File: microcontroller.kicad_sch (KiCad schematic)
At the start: 6 parts

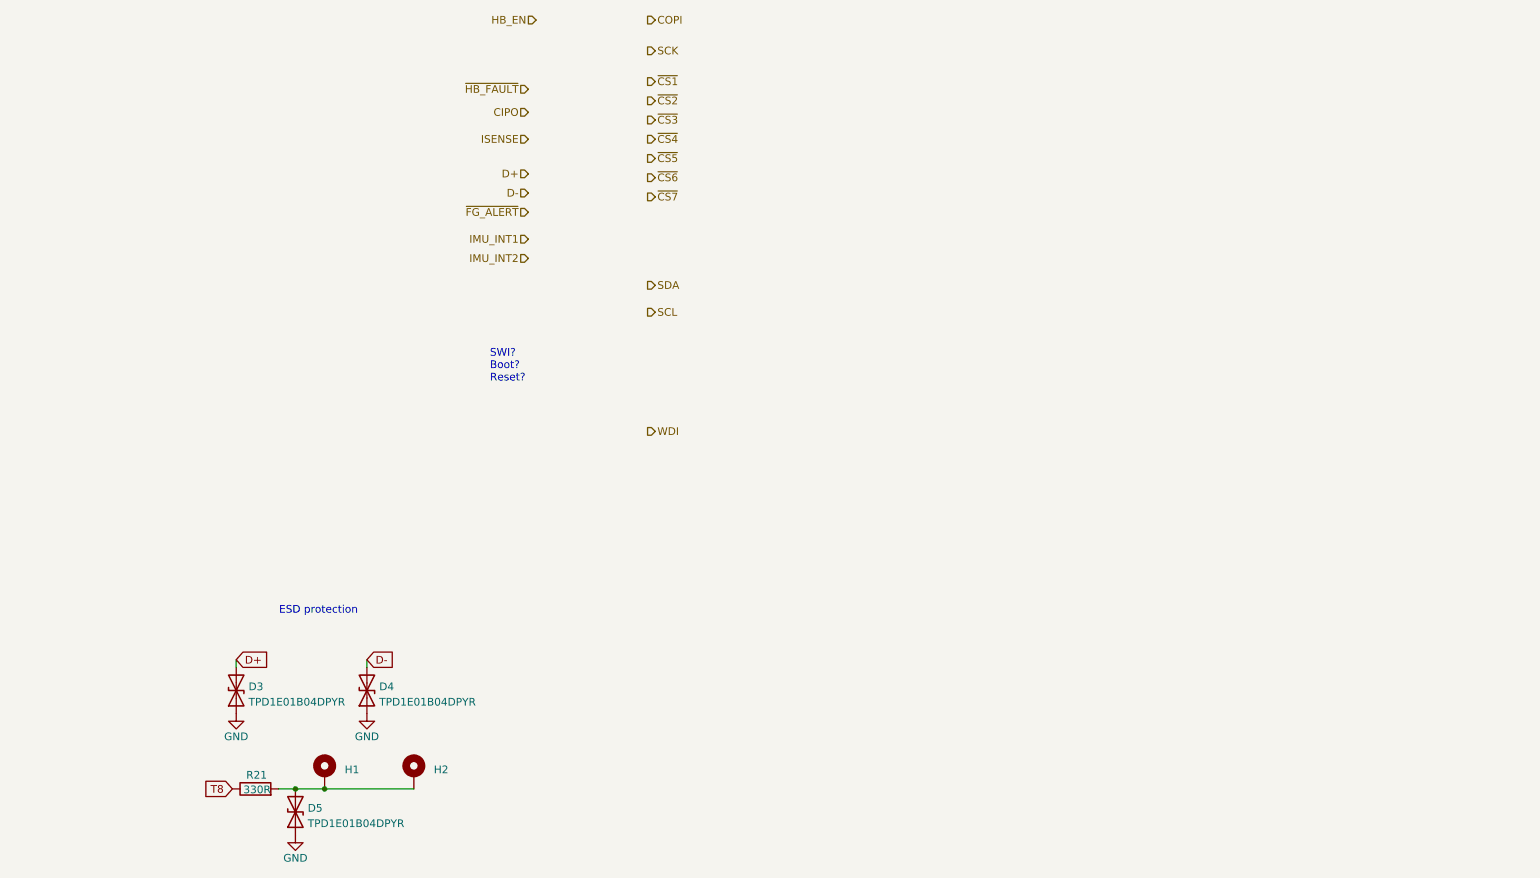
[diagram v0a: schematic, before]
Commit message: schematic rough draft except fpc
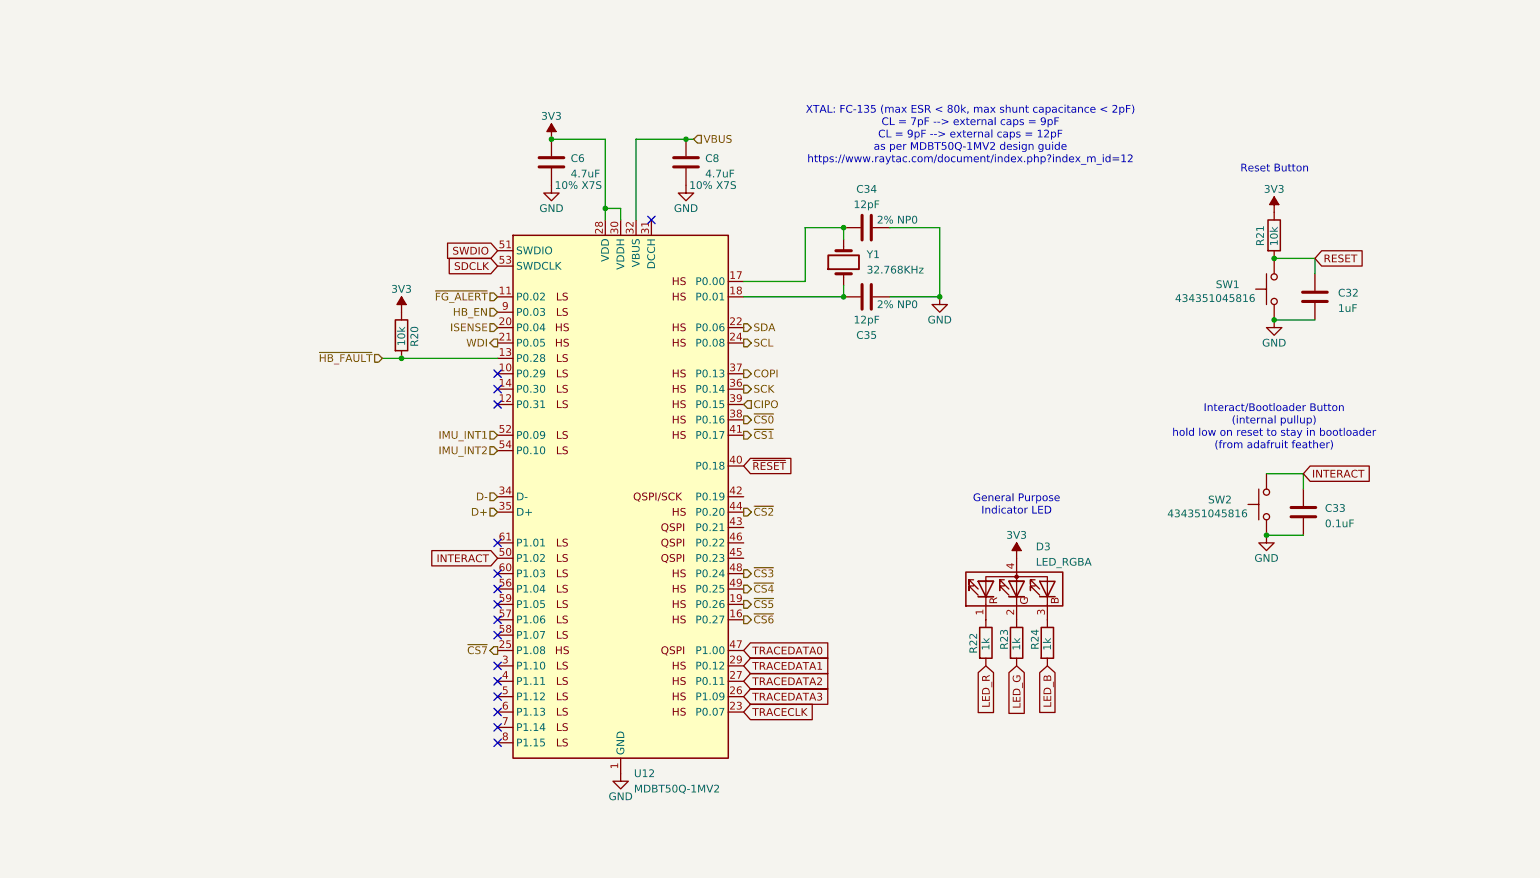
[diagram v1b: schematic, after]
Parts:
- removed D3, D4, D5: TPD1E01B04DPYR, v12e:X1-SON-2(0.6x1), symbol Device:D_TVS
- removed H1, H2: MountingHole_Pad, v12e:MountingHole_1.8mm_M1.6_Pad_TopBottom, symbol Mechanical:MountingHole_Pad
- added C32: 1uF, Capacitor_SMD:C_0402_1005Metric, symbol Device:C
- added C33: 0.1uF, Capacitor_SMD:C_0402_1005Metric, symbol Device:C
- added C34, C35: 12pF, symbol Device:C
- added C6, C8: 4.7uF, Capacitor_SMD:C_0603_1608Metric, symbol Device:C
- added D3: LED_RGBA, v12e:RGBA_LTST-S310F3WT, symbol Device:LED_RGBA
- added R20: 10k, Resistor_SMD:R_0402_1005Metric, symbol Device:R
- added R22, R23, R24: 1k, Resistor_SMD:R_0402_1005Metric, symbol Device:R
- added SW1, SW2: 434351045816, v12e:SW_Wurth_434351045816, symbol Switch:SW_Push
- added U12: MDBT50Q-1MV2, RF_Module:Raytac_MDBT50Q, symbol RF_Module:MDBT50Q-1MV2
- added Y1: 32.768KHz, Crystal:Crystal_SMD_3215-2Pin_3.2x1.5mm, symbol Device:Crystal
- R21: value 330R -> 10k; JLCPCB Part # C25104 -> C25744
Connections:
- net CIPO: now also U12.39 (P0.15)
- net COPI: now also U12.37 (P0.13)
- net D+: now also U12.35 (D+)
- net D-: now also U12.34 (D-)
- net GND: now also C32.2, C33.2, C34.2, C35.1, C6.2, C8.2, SW1.1, SW2.1, U12.1 (GND), U12.15 (GND), U12.2 (GND), U12.33 (GND), U12.55 (GND)
- net HB_EN: now also U12.9 (P0.03)
- net IMU_INT1: now also U12.52 (P0.09)
- net IMU_INT2: now also U12.54 (P0.10)
- net ISENSE: now also U12.20 (P0.04)
- net SCK: now also U12.36 (P0.14)
- net SCL: now also U12.24 (P0.08)
- net SDA: now also U12.22 (P0.06)
- net WDI: now also U12.21 (P0.05)
- net ~{CS1}: now also U12.41 (P0.17)
- net ~{CS2}: now also U12.44 (P0.20)
- net ~{CS3}: now also U12.48 (P0.24)
- net ~{CS4}: now also U12.49 (P0.25)
- net ~{CS5}: now also U12.19 (P0.26)
- net ~{CS6}: now also U12.16 (P0.27)
- net ~{CS7}: now also U12.25 (P1.08)
- net ~{FG_ALERT}: now also U12.11 (P0.02)
- net ~{HB_FAULT}: now also R20.2, U12.13 (P0.28)
- net RESET: now reaches R21.2
- net RESET: now also C32.1, SW1.2
- net T8 renamed 3V3
- net 3V3: now also C6.1, D3.4 (A), R20.1, U12.28 (VDD), U12.30 (VDDH)
- new net: D3.1 (RK), R22.1
- new net: C35.2, U12.18 (P0.01), Y1.1
- new net: C34.1, U12.17 (P0.00), Y1.2
- new net: D3.2 (GK), R23.1
- new net: D3.3 (BK), R24.1
- new net INTERACT: C33.1, SW2.2, U12.50 (P1.02)
- new net LED_B: R24.2
- new net LED_G: R23.2
- new net LED_R: R22.2
- new net SDCLK: U12.53 (SWDCLK)
- new net SWDIO: U12.51 (SWDIO)
- new net TRACECLK: U12.23 (P0.07)
- new net TRACEDATA0: U12.47 (P1.00)
- new net TRACEDATA1: U12.29 (P0.12)
- new net TRACEDATA2: U12.27 (P0.11)
- new net TRACEDATA3: U12.26 (P1.09)
- new net VBUS: C8.1, U12.32 (VBUS)
- new net ~{CS0}: U12.38 (P0.16)
- new net ~{RESET}: U12.40 (P0.18)
- no-connect marks 0 -> 16
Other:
- note added: "General Purpose Indicator LED"
- note added: "Interact/Bootloader Button (internal pullup) hold low on reset to stay in bootloader (from adafruit feather)"
- note added: "Reset Button"
- note added: "XTAL: FC-135 (max ESR < 80k, max shunt capacitance < 2pF) CL = 7pF --> external caps = 9pF CL = 9pF --> external caps = 12pF as per MDBT50Q-1MV2 design guide https://www.raytac.com/document/index.php?index_m_id=12"
- note removed: "ESD protection"
- note removed: "SWI? Boot? Reset?"

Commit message: schematic draft 2; no FPC connections, no testpoints
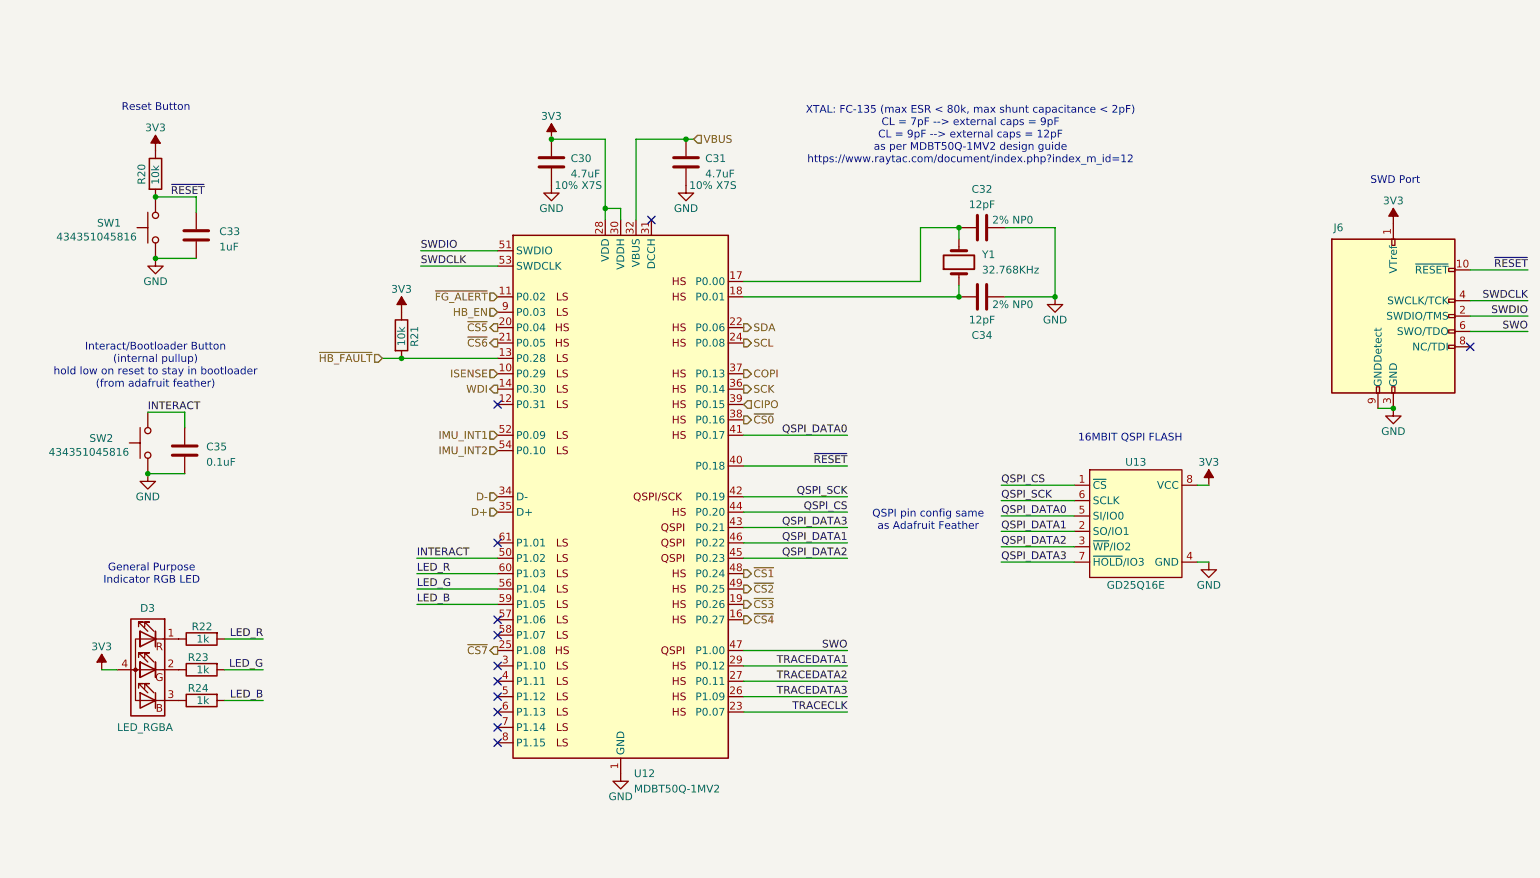
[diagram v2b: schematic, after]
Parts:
- added J6: Conn_ARM_JTAG_SWD_10, nrf52-controller:SWD_2x10_target-pads, symbol Connector:Conn_ARM_JTAG_SWD_10
- added U13: GD25Q16E, nrf52-controller:WSON-8_3x2mm_EP-0.2x2mm, symbol nrf52-controller:GD25Q16E
- C32: renamed from C34; footprint (none) -> Capacitor_SMD:C_0402_1005Metric
- C34: renamed from C35; footprint (none) -> Capacitor_SMD:C_0402_1005Metric
- D3: footprint v12e:RGBA_LTST-S310F3WT -> nrf52-controller:RGBA_LTST-S310F3WT
- SW1, SW2: footprint v12e:SW_Wurth_434351045816 -> nrf52-controller:SW_Wurth_434351045816
- renumbered C6 to C30, C8 to C31, C32 to C33, C33 to C35, R21 to R20, R20 to R21
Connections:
- net RESET is gone; now on net ~{RESET}: C33.1, R20.2, SW1.2
- net 3V3: now also J6.1 (VTref), U13.8 (VCC)
- net GND: now also J6.3 (GND), J6.5 (GND), J6.9 (GNDDetect), U13.4 (GND), U13.9 (EPAD)
- net ISENSE: now also U12.10 (P0.29); no longer U12.20 (P0.04)
- net LED_B: now also U12.59 (P1.05)
- net LED_G: now also U12.56 (P1.04)
- net LED_R: now also U12.60 (P1.03)
- net SWDIO: now also J6.2 (SWDIO/TMS)
- net WDI: now also U12.14 (P0.30); no longer U12.21 (P0.05)
- net ~{CS1}: now also U12.48 (P0.24); no longer U12.41 (P0.17)
- net ~{CS2}: now also U12.49 (P0.25); no longer U12.44 (P0.20)
- net ~{CS3}: now also U12.19 (P0.26); no longer U12.48 (P0.24)
- net ~{CS4}: now also U12.16 (P0.27); no longer U12.49 (P0.25)
- net ~{CS5}: now also U12.20 (P0.04); no longer U12.19 (P0.26)
- net ~{CS6}: now also U12.21 (P0.05); no longer U12.16 (P0.27)
- net ~{RESET}: now also J6.10 (~{RESET})
- net QSPI_SCK: now reaches U12.42 (P0.19)
- net QSPI_SCK: now also U13.6 (SCLK)
- net QSPI_DATA3: now reaches U12.43 (P0.21)
- net QSPI_DATA3: now also U13.7 (~{HOLD}/IO3)
- net QSPI_DATA2: now reaches U12.45 (P0.23)
- net QSPI_DATA2: now also U13.3 (~{WP}/IO2)
- net QSPI_DATA1: now reaches U12.46 (P0.22)
- net QSPI_DATA1: now also U13.2 (SO/IO1)
- net SDCLK renamed SWDCLK
- net SWDCLK: now also J6.4 (SWCLK/TCK)
- net TRACEDATA0 renamed SWO
- net SWO: now also J6.6 (SWO/TDO)
- new net QSPI_CS: U12.44 (P0.20), U13.1 (~{CS})
- new net QSPI_DATA0: U12.41 (P0.17), U13.5 (SI/IO0)
- no-connect marks 16 -> 12
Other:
- note added: "16MBIT QSPI FLASH"
- note added: "General Purpose Indicator RGB LED"
- note added: "QSPI pin config same as Adafruit Feather"
- note added: "SWD Port"
- note removed: "General Purpose Indicator LED"
- moved on the sheet: C32, C33, C34, C35, D3, R20, R22, R23, R24, SW1, SW2, Y1

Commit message: layout start
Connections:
- net XTAL2: now reaches C34.2, U12.18 (P0.01)
- net XTAL2: now also Y1.2; no longer Y1.1
- net XTAL1: now reaches C32.1, U12.17 (P0.00)
- net XTAL1: now also Y1.1; no longer Y1.2
- net 12V_EN1: now reaches U12.57 (P1.06)
- no-connect marks 12 -> 11
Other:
- moved on the sheet: Y1
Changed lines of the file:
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@@
-	)
-	(no_connect
-		(at 97.155 134.62)
 	)
 	(no_connect
@@
 		)
 	)
+	(label "XTAL1"
+		(at 149.86 78.74 0)
+		(fields_autoplaced yes)
+		(effects
+			(font
+				(size 1.27 1.27)
+			)
+			(justify left bottom)
+		)
+	)
 	(label "LED_B"
 		(at 58.42 147.955 180)
@@
 			)
 			(justify right bottom)
+		)
+	)
+	(label "XTAL2"
+		(at 149.86 81.28 0)
+		(fields_autoplaced yes)
+		(effects
+			(font
+				(size 1.27 1.27)
+			)
+			(justify left bottom)
 		)
 	)
@@
 		(shape output)
 		(at 97.155 88.9 180)
+		(fields_autoplaced yes)
+		(effects
+			(font
+				(size 1.27 1.27)
+			)
+			(justify right)
+		)
+	)
+	(hierarchical_label "12V_EN1"
+		(shape output)
+		(at 97.155 134.62 180)
 		(fields_autoplaced yes)
 		(effects
@@
 	(symbol
 		(lib_id "Device:Crystal")
-		(at 173.355 75.565 90)
+		(at 173.355 75.565 270)
 		(unit 1)
 		(exclude_from_sim no)
@@
 		(fields_autoplaced yes)
 		(property "Reference" "Y1"
-			(at 177.165 74.2949 90)
-			(effects
-				(font
-					(size 1.27 1.27)
-				)
-				(justify right)
+			(at 177.8 74.2949 90)
+			(effects
+				(font
+					(size 1.27 1.27)
+				)
+				(justify left)
 			)
 		)
 		(property "Value" "32.768KHz"
-			(at 177.165 76.8349 90)
-			(effects
-				(font
-					(size 1.27 1.27)
-				)
-				(justify right)
-			)
-		)
+			(at 177.8 76.8349 90)
+			(effects
+				(font
+					(size 1.27 1.27)
+				)
+				(justify left)
+			)
+		)
